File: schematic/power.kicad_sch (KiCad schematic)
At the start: 13 parts, among them J7 12V INPUT, U3 AP63205WU-7, U4 AP2112K-3.3TRG1

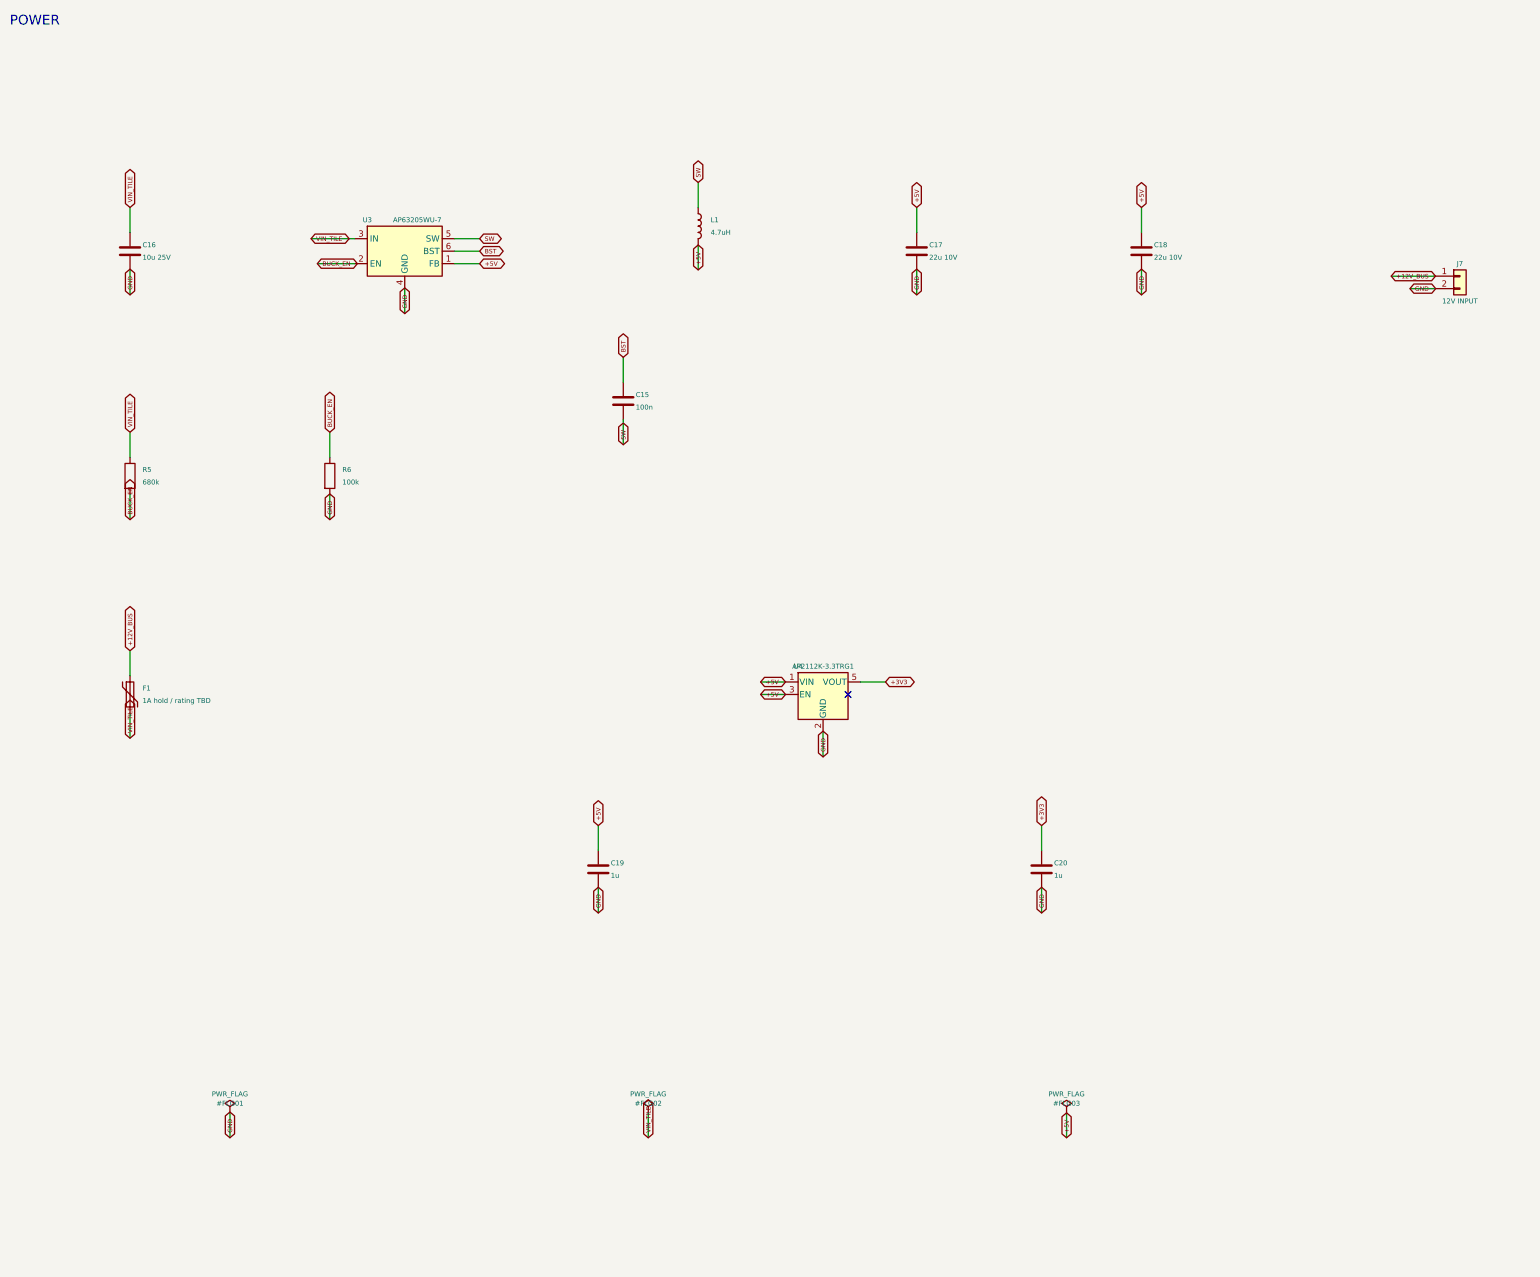
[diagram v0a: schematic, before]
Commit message: finish tile schematics and connector footprints
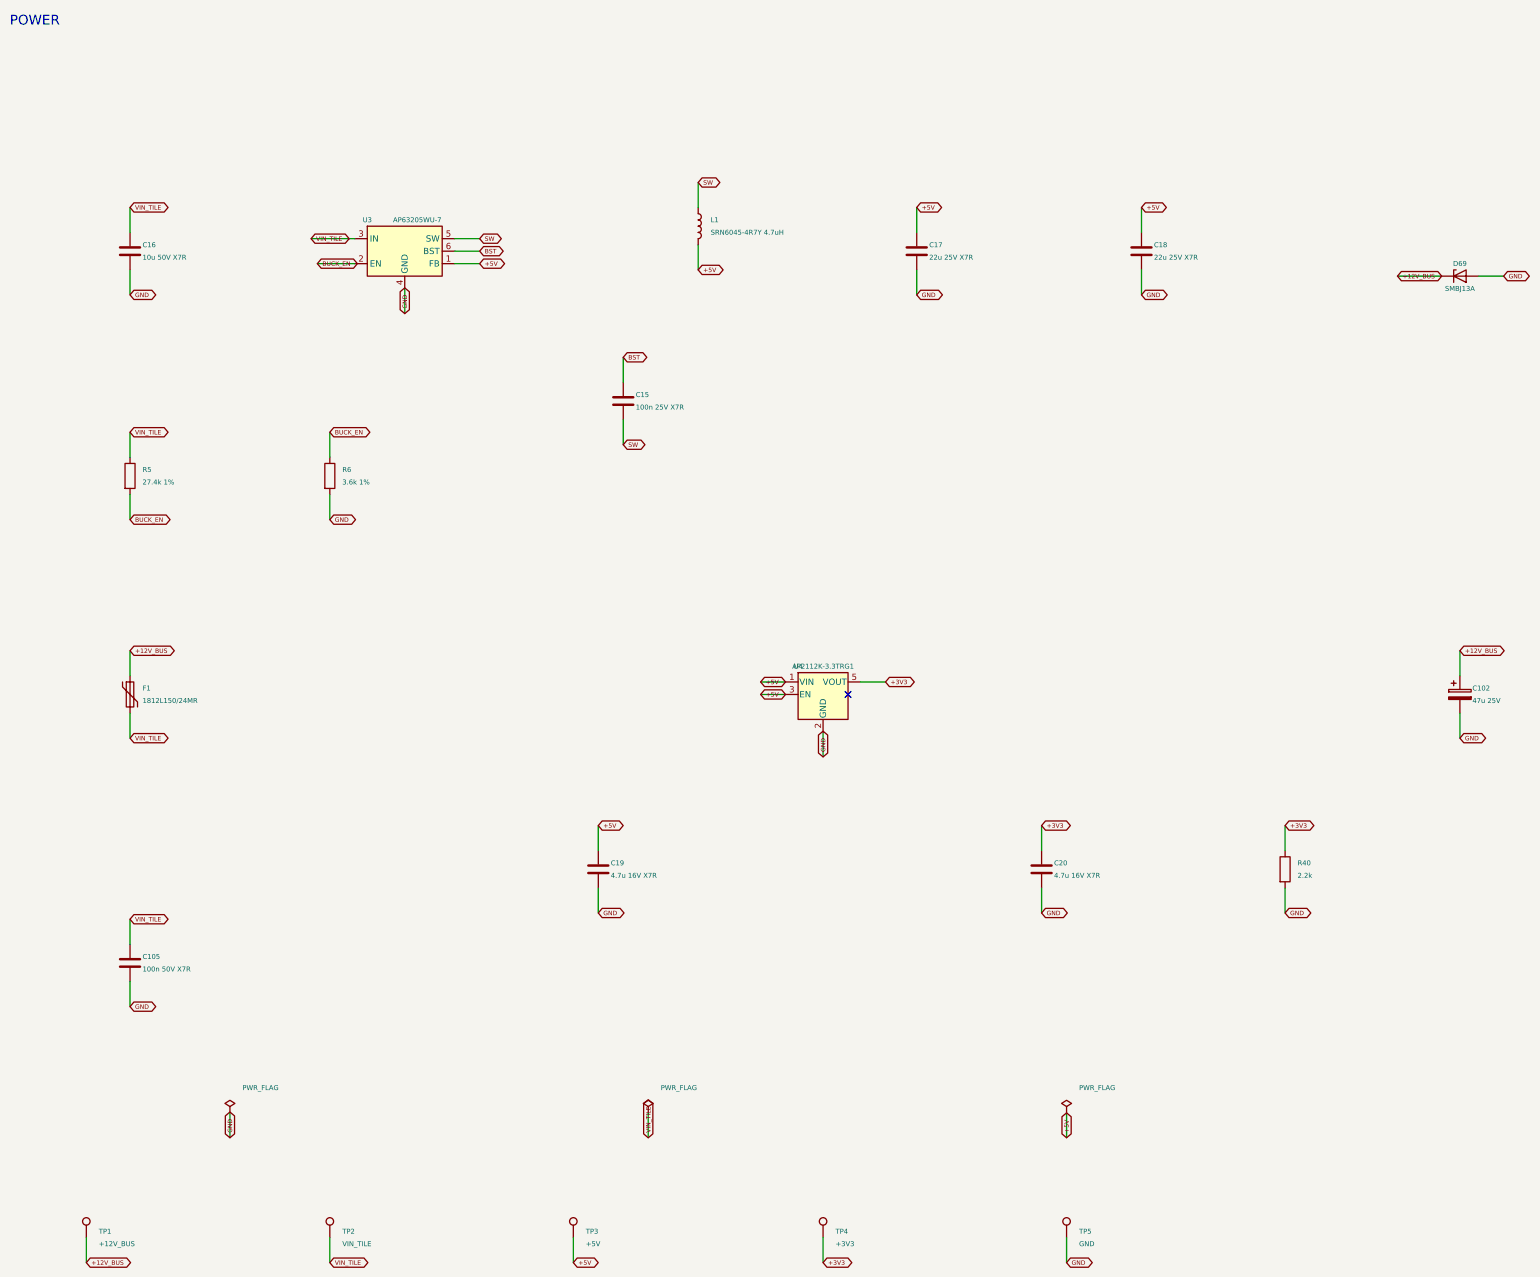
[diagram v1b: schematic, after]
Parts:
- removed J7: 12V INPUT, TerminalBlock_Phoenix:TerminalBlock_Phoenix_MKDS-1,5-2-5.08_1x02_P5.08mm_Horizontal, symbol Connector_Generic:Conn_01x02
- added C102: 47u 25V, Capacitor_SMD:CP_Elec_5x5.8, symbol Device:C_Polarized
- added C105: 100n 50V X7R, Capacitor_SMD:C_0603_1608Metric, symbol Device:C
- added D69: SMBJ13A, Diode_SMD:D_SMB, symbol Device:D_Zener
- added R40: 2.2k, Resistor_SMD:R_0603_1608Metric, symbol Device:R
- added TP1: +12V_BUS, TestPoint:TestPoint_Pad_D1.5mm, symbol Connector:TestPoint
- added TP2: VIN_TILE, TestPoint:TestPoint_Pad_D1.5mm, symbol Connector:TestPoint
- added TP3: +5V, TestPoint:TestPoint_Pad_D1.5mm, symbol Connector:TestPoint
- added TP4: +3V3, TestPoint:TestPoint_Pad_D1.5mm, symbol Connector:TestPoint
- added TP5: GND, TestPoint:TestPoint_Pad_D1.5mm, symbol Connector:TestPoint
- C15: value 100n -> 100n 25V X7R; MPN (none) -> C0603C104K3RACTU; Manufacturer (none) -> KEMET
- C16: value 10u 25V -> 10u 50V X7R; footprint Capacitor_SMD:C_1206_3216Metric -> Capacitor_SMD:C_1210_3225Metric; MPN (none) -> C1210C106K5RACTU; Manufacturer (none) -> KEMET
- C17, C18: value 22u 10V -> 22u 25V X7R; footprint Capacitor_SMD:C_1206_3216Metric -> Capacitor_SMD:C_1210_3225Metric; MPN (none) -> C1210C226K3RACTU; Manufacturer (none) -> KEMET
- C19, C20: value 1u -> 4.7u 16V X7R; footprint Capacitor_SMD:C_0603_1608Metric -> Capacitor_SMD:C_0805_2012Metric; MPN (none) -> C0805C475K4RACTU; Manufacturer (none) -> KEMET
- F1: value 1A hold / rating TBD -> 1812L150/24MR; MPN (none) -> 1812L150/24MR; Manufacturer (none) -> Littelfuse
- L1: value 4.7uH -> SRN6045-4R7Y 4.7uH; footprint Inductor_SMD:L_6.3x6.3_H3 -> RGB_Tiles:L_Bourns_SRN6045; MPN (none) -> SRN6045-4R7Y; Manufacturer (none) -> Bourns
- R5: value 680k -> 27.4k 1%; MPN (none) -> RC0603FR-0727K4L; Manufacturer (none) -> Yageo; Power (none) -> 0.1W; Tolerance (none) -> 1%
- R6: value 100k -> 3.6k 1%; MPN (none) -> RC0603FR-073K6L; Manufacturer (none) -> Yageo; Power (none) -> 0.1W; Tolerance (none) -> 1%
- U3: MPN (none) -> AP63205WU-7; Manufacturer (none) -> Diodes Incorporated
- U4: MPN (none) -> AP2112K-3.3TRG1; Manufacturer (none) -> Diodes Incorporated
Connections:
- net +12V_BUS: now also C102.1, D69.1 (K), TP1.1
- net +3V3: now also R40.1, TP4.1
- net +5V: now also TP3.1
- net GND: now also C102.2, C105.2, D69.2 (A), R40.2, TP5.1
- net VIN_TILE: now also C105.1, TP2.1

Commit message: add firmware, controller and manufacturing files
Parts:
- C15: MPN C0603C104K3RACTU -> CL10B104KA8NNNC; Manufacturer KEMET -> Samsung Electro-Mechanics
- C16: MPN C1210C106K5RACTU -> CL32B106KBJNNNE; Manufacturer KEMET -> Samsung Electro-Mechanics
- C17, C18: MPN C1210C226K3RACTU -> CL32B226KAJNNNE; Manufacturer KEMET -> Samsung Electro-Mechanics
- R6: MPN RC0603FR-073K6L -> RC0603FR-133K6L
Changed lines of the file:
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@@
 			)
 		)
-		(property "Datasheet" "https://search.kemet.com/component-documentation/download/specsheet/C0603C104K3RACTU"
+		(property "Datasheet" "https://product.samsungsem.com/mlcc/CL10B104KA8NNN.do"
 			(at 144.78 95.25 0)
 			(effects
@@
 			)
 		)
-		(property "Manufacturer" "KEMET"
+		(property "Manufacturer" "Samsung Electro-Mechanics"
 			(at 144.78 95.25 0)
 			(effects
@@
 			)
 		)
-		(property "MPN" "C0603C104K3RACTU"
+		(property "MPN" "CL10B104KA8NNNC"
 			(at 144.78 95.25 0)
 			(effects
@@
 			)
 		)
-		(property "Datasheet" "https://search.kemet.com/component-documentation/download/specsheet/C1210C106K5RACTU"
+		(property "Datasheet" "https://product.samsungsem.com/mlcc/CL32B106KBJNNN.do"
 			(at 44.45 64.77 0)
 			(effects
@@
 			)
 		)
-		(property "Manufacturer" "KEMET"
+		(property "Manufacturer" "Samsung Electro-Mechanics"
 			(at 44.45 64.77 0)
 			(effects
@@
 			)
 		)
-		(property "MPN" "C1210C106K5RACTU"
+		(property "MPN" "CL32B106KBJNNNE"
 			(at 44.45 64.77 0)
 			(effects
@@
 			)
 		)
-		(property "Datasheet" "https://search.kemet.com/component-documentation/download/specsheet/C1210C226K3RACTU"
+		(property "Datasheet" "https://product.samsungsem.com/mlcc/CL32B226KAJNNN.do"
 			(at 204.47 64.77 0)
 			(effects
@@
 			)
 		)
-		(property "Manufacturer" "KEMET"
+		(property "Manufacturer" "Samsung Electro-Mechanics"
 			(at 204.47 64.77 0)
 			(effects
@@
 			)
 		)
-		(property "MPN" "C1210C226K3RACTU"
+		(property "MPN" "CL32B226KAJNNNE"
 			(at 204.47 64.77 0)
 			(effects
@@
 			)
 		)
-		(property "Datasheet" "https://search.kemet.com/component-documentation/download/specsheet/C1210C226K3RACTU"
+		(property "Datasheet" "https://product.samsungsem.com/mlcc/CL32B226KAJNNN.do"
 			(at 250.19 64.77 0)
 			(effects
@@
 			)
 		)
-		(property "Manufacturer" "KEMET"
+		(property "Manufacturer" "Samsung Electro-Mechanics"
 			(at 250.19 64.77 0)
 			(effects
@@
 			)
 		)
-		(property "MPN" "C1210C226K3RACTU"
+		(property "MPN" "CL32B226KAJNNNE"
 			(at 250.19 64.77 0)
 			(effects
@@
 			)
 		)
-		(property "Datasheet" ""
+		(property "Datasheet" "https://www.yageo.com/upload/media/product/productsearch/datasheet/rchip/PYu-RC_Group_51_RoHS_L.pdf"
 			(at 85.09 110.49 0)
 			(effects
@@
 			)
 		)
-		(property "MPN" "RC0603FR-073K6L"
+		(property "MPN" "RC0603FR-133K6L"
 			(at 85.09 110.49 0)
 			(effects
